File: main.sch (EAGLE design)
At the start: 28 parts, among them U1 MCP2551P-SOCKET, U2 STN1110SOCKET-28, Y1 16Mhz

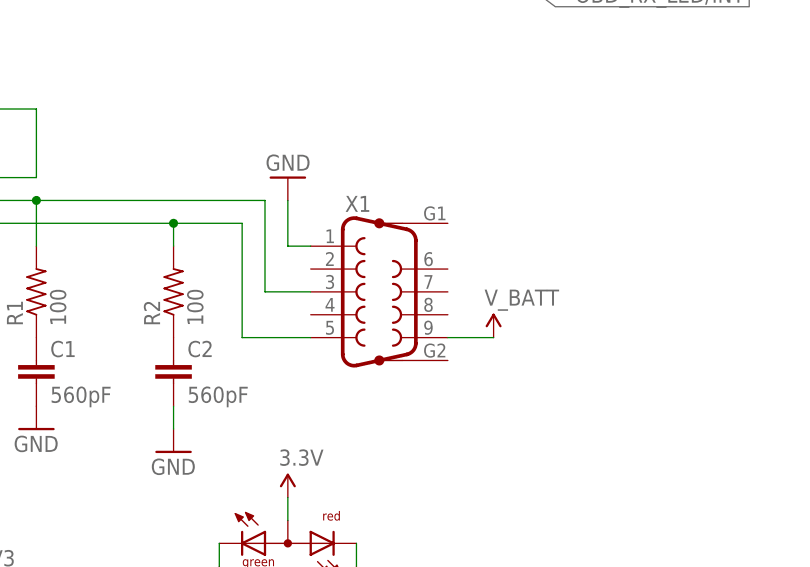
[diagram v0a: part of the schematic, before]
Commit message: Added some space and better routing
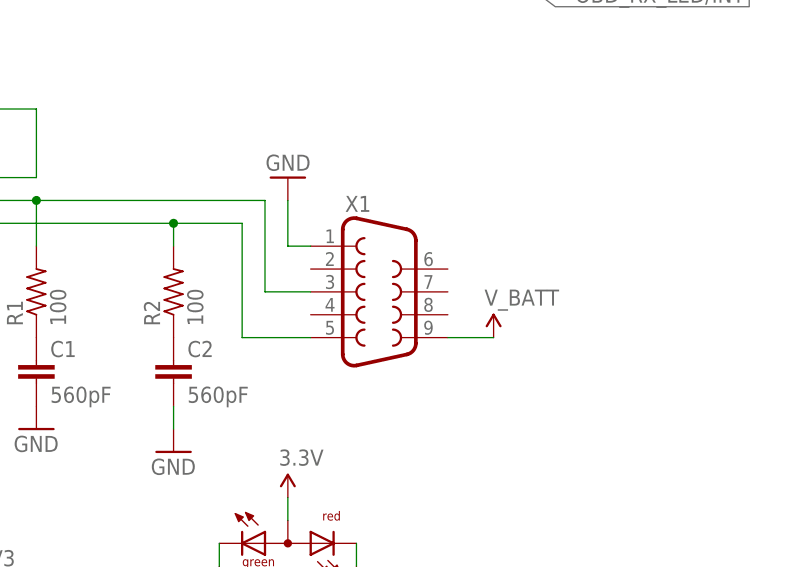
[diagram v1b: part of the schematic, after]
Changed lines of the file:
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@@
 <parts>
 <part name="ARDUINO1" library="post7_arduino" deviceset="ARDUINO" device=""/>
-<part name="X1" library="con-subd" deviceset="F09HP" device=""/>
+<part name="X1" library="con-subd" deviceset="F09" device="HP"/>
 <part name="GND28" library="SparkFun" deviceset="GND" device=""/>
 <part name="GND15" library="SparkFun" deviceset="GND" device=""/>

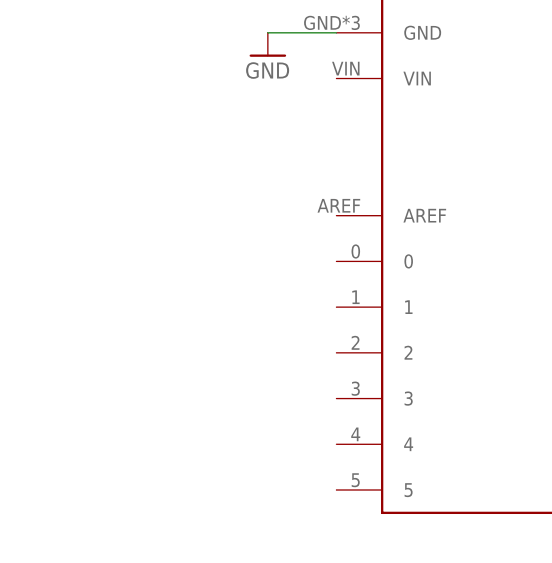
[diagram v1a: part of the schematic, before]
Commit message: Improved routing, added micro-sd slot
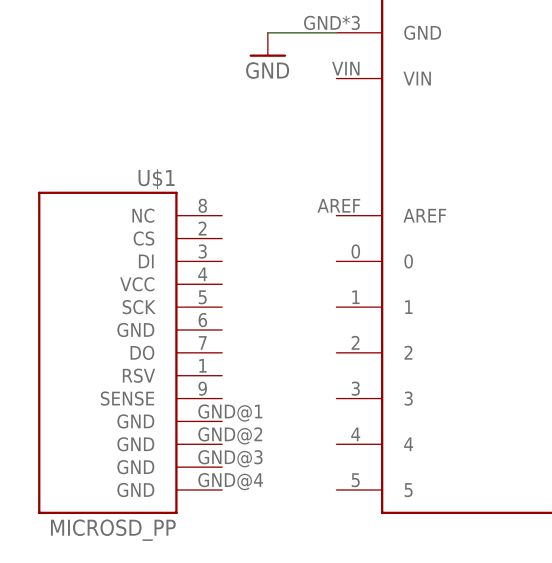
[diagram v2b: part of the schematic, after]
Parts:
- added U$1: MICROSD_PP, DE1594-v2:MICROSD_PP
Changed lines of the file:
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@@
 <part name="SUPPLY14" library="SparkFun-Aesthetics" deviceset="3.3V" device=""/>
 <part name="GND11" library="SparkFun-Aesthetics" deviceset="GND" device=""/>
+<part name="U$1" library="DE1594-v2" deviceset="MICROSD_PP" device=""/>
 </parts>
 <sheets>
@@
 <instance part="SUPPLY14" gate="G$1" x="-12.7" y="78.74"/>
 <instance part="GND11" gate="1" x="-12.7" y="68.58"/>
+<instance part="U$1" gate="G$1" x="-20.32" y="17.78"/>
 </instances>
 <busses>

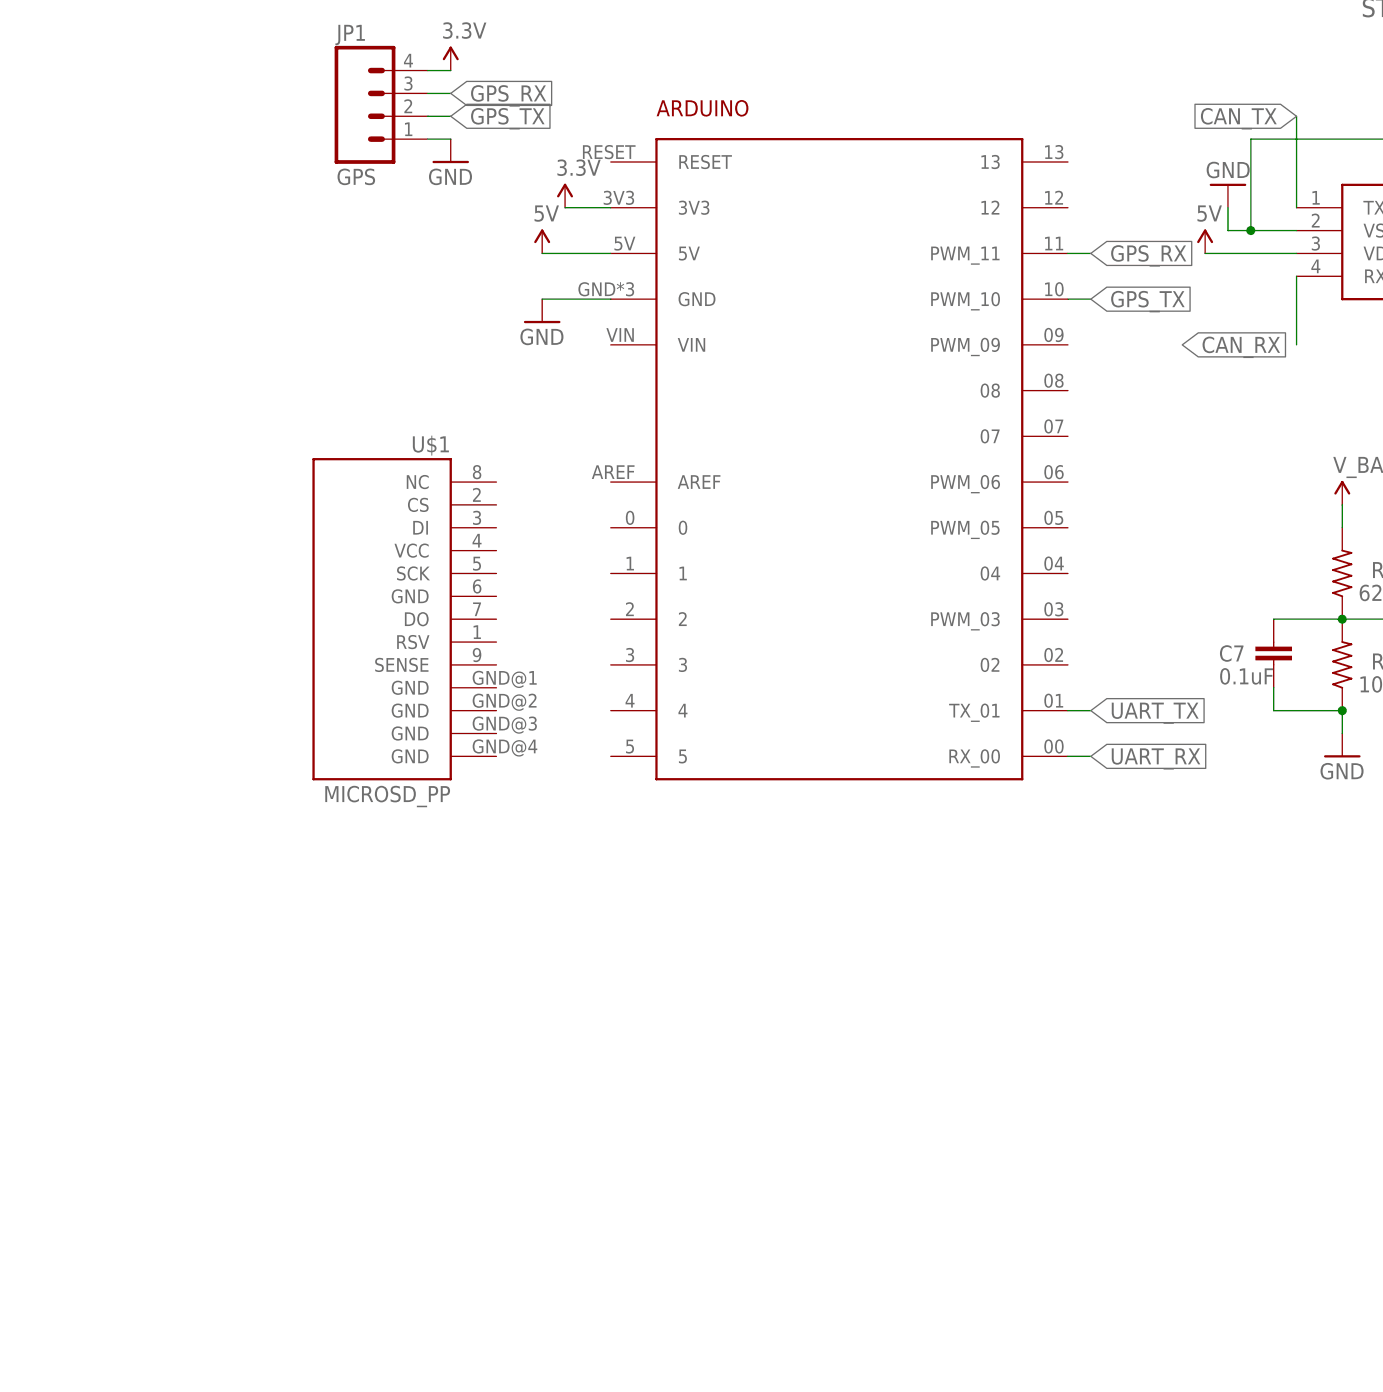
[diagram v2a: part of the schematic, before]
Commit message: Wired the SD card and level shifter
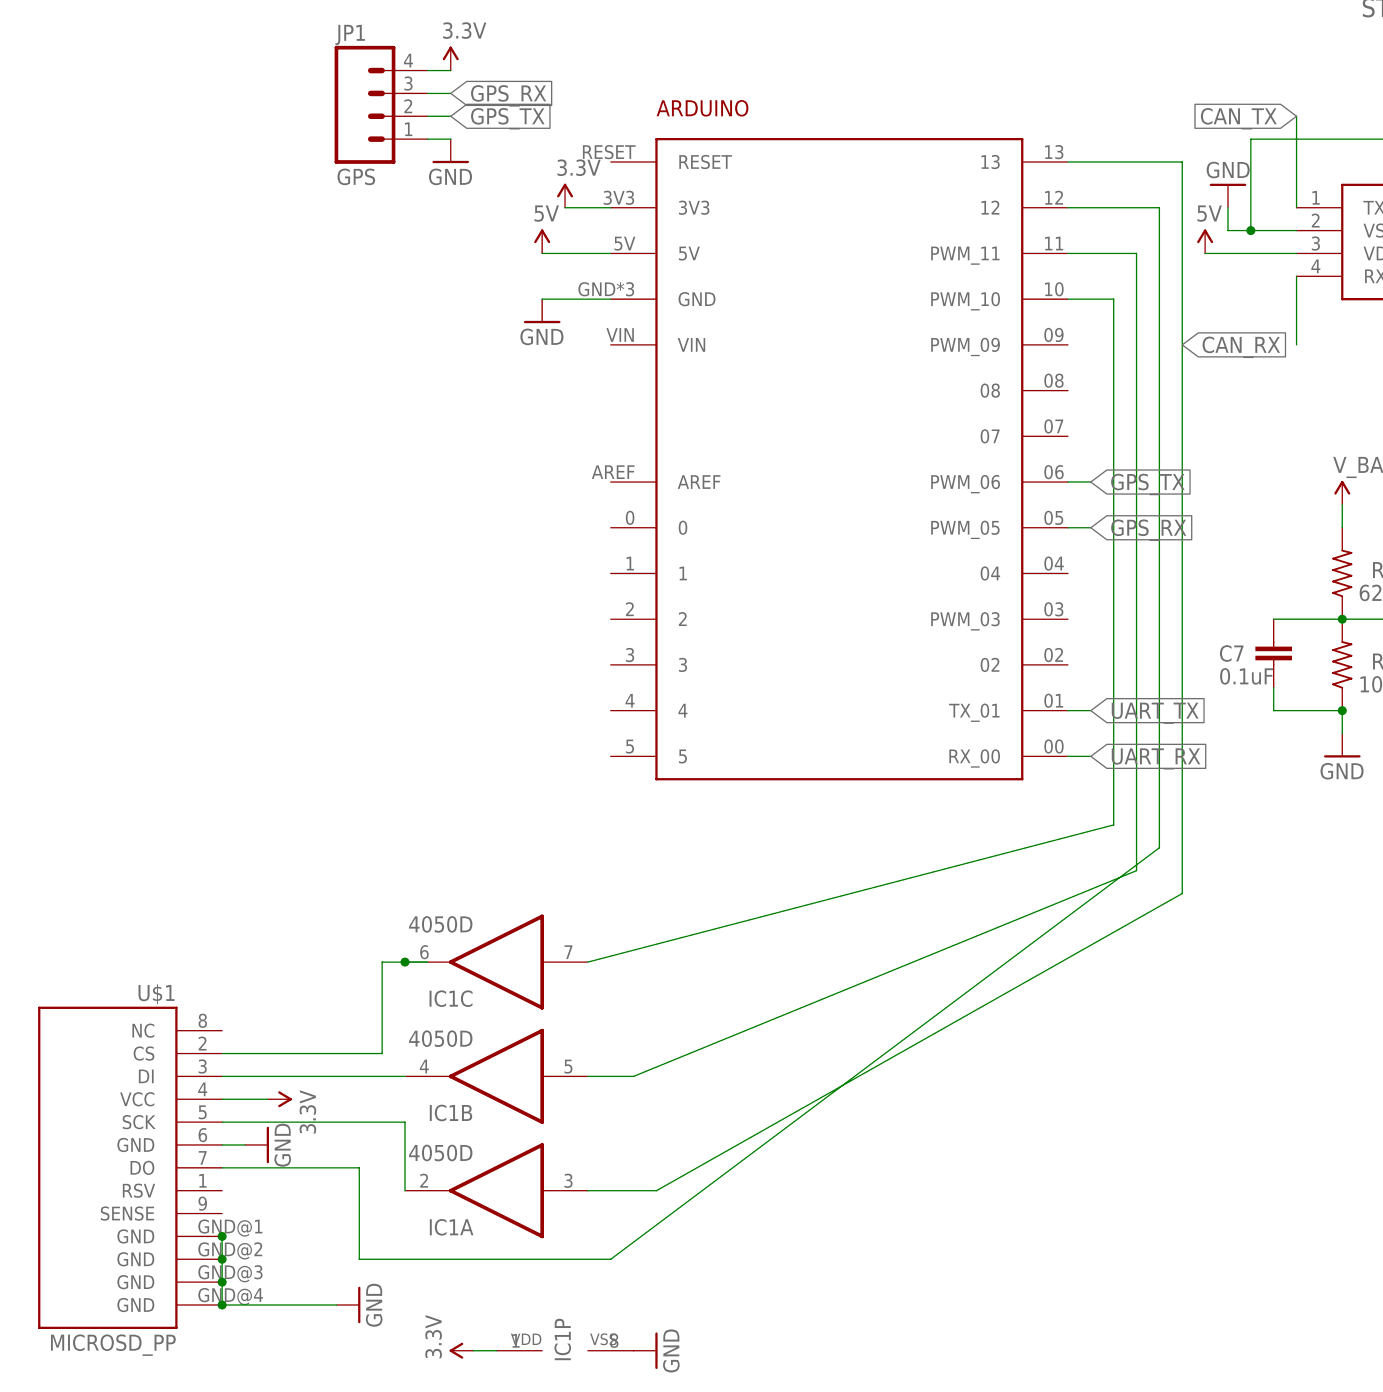
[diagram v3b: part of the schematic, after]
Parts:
- added IC1: 4050D, 40xx:4050D
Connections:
- new net N$13: IC1B.O, U$1.DI
- new net N$15: IC1C.O, U$1.CS
- new net N$16: ARDUINO1.13, IC1A.I
- new net N$17: IC1A.O, U$1.SCK
- new net N$18: ARDUINO1.PWM_10, IC1C.I
- new net N$19: ARDUINO1.12, U$1.DO
- new net N$20: ARDUINO1.PWM_11, IC1B.I
- net 3.3V: now also IC1P.VDD, U$1.VCC
- net GND: now also IC1P.VSS, U$1.GND, U$1.GND@1, U$1.GND@2, U$1.GND@3, U$1.GND@4
- net GPS_RX: now also ARDUINO1.PWM_05; no longer ARDUINO1.PWM_11
- net GPS_TX: now also ARDUINO1.PWM_06; no longer ARDUINO1.PWM_10
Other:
- moved on the sheet: U$1
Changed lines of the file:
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@@
 <part name="GND11" library="SparkFun-Aesthetics" deviceset="GND" device=""/>
 <part name="U$1" library="DE1594-v2" deviceset="MICROSD_PP" device=""/>
+<part name="IC1" library="40xx" deviceset="4050" device="D" value="4050D"/>
+<part name="SUPPLY15" library="SparkFun-Aesthetics" deviceset="3.3V" device=""/>
+<part name="GND12" library="SparkFun-Aesthetics" deviceset="GND" device=""/>
+<part name="GND13" library="SparkFun-Aesthetics" deviceset="GND" device=""/>
+<part name="SUPPLY16" library="SparkFun-Aesthetics" deviceset="3.3V" device=""/>
+<part name="GND14" library="SparkFun-Aesthetics" deviceset="GND" device=""/>
 </parts>
 <sheets>
@@
 <instance part="SUPPLY14" gate="G$1" x="-12.7" y="78.74"/>
 <instance part="GND11" gate="1" x="-12.7" y="68.58"/>
-<instance part="U$1" gate="G$1" x="-20.32" y="17.78"/>
+<instance part="U$1" gate="G$1" x="-50.8" y="-43.18"/>
+<instance part="IC1" gate="A" x="-7.62" y="-45.72" rot="R180"/>
+<instance part="IC1" gate="B" x="-7.62" y="-33.02" rot="R180"/>
+<instance part="IC1" gate="C" x="-7.62" y="-20.32" rot="R180"/>
+<instance part="IC1" gate="P" x="0" y="-63.5" rot="R90"/>
+<instance part="SUPPLY15" gate="G$1" x="-10.16" y="-63.5" rot="R90"/>
+<instance part="GND12" gate="1" x="10.16" y="-63.5" rot="R90"/>
+<instance part="GND13" gate="1" x="-22.86" y="-58.42" rot="R90"/>
+<instance part="SUPPLY16" gate="G$1" x="-33.02" y="-35.56" rot="R270"/>
+<instance part="GND14" gate="1" x="-33.02" y="-40.64" rot="R90"/>
 </instances>
 <busses>
@@
 <pinref part="GND11" gate="1" pin="GND"/>
 </segment>
+<segment>
+<pinref part="IC1" gate="P" pin="VSS"/>
+<pinref part="GND12" gate="1" pin="GND"/>
+</segment>
+<segment>
+<pinref part="U$1" gate="G$1" pin="GND@1"/>
+<wire x1="-38.1" y1="-50.8" x2="-38.1" y2="-53.34" width="0.1524" layer="91"/>
+<pinref part="GND13" gate="1" pin="GND"/>
+<pinref part="U$1" gate="G$1" pin="GND@2"/>
+<junction x="-38.1" y="-53.34"/>
+<wire x1="-38.1" y1="-53.34" x2="-38.1" y2="-55.88" width="0.1524" layer="91"/>
+<pinref part="U$1" gate="G$1" pin="GND@3"/>
+<junction x="-38.1" y="-55.88"/>
+<wire x1="-38.1" y1="-55.88" x2="-38.1" y2="-58.42" width="0.1524" layer="91"/>
+<pinref part="U$1" gate="G$1" pin="GND@4"/>
+<junction x="-38.1" y="-58.42"/>
+<wire x1="-38.1" y1="-58.42" x2="-25.4" y2="-58.42" width="0.1524" layer="91"/>
+<junction x="-38.1" y="-50.8"/>
+</segment>
+<segment>
+<pinref part="U$1" gate="G$1" pin="GND"/>
+<pinref part="GND14" gate="1" pin="GND"/>
+<wire x1="-38.1" y1="-40.64" x2="-35.56" y2="-40.64" width="0.1524" layer="91"/>
+</segment>
 </net>
 <net name="N$1" class="0">
@@
 <wire x1="-15.24" y1="78.74" x2="-12.7" y2="78.74" width="0.1524" layer="91"/>
 <pinref part="SUPPLY14" gate="G$1" pin="3.3V"/>
+</segment>
+<segment>
+<pinref part="IC1" gate="P" pin="VDD"/>
+<pinref part="SUPPLY15" gate="G$1" pin="3.3V"/>
+<wire x1="-10.16" y1="-63.5" x2="-7.62" y2="-63.5" width="0.1524" layer="91"/>
+</segment>
+<segment>
+<pinref part="U$1" gate="G$1" pin="VCC"/>
+<pinref part="SUPPLY16" gate="G$1" pin="3.3V"/>
+<wire x1="-38.1" y1="-35.56" x2="-33.02" y2="-35.56" width="0.1524" layer="91"/>
 </segment>
 </net>
@@
 </segment>
 <segment>
-<pinref part="ARDUINO1" gate="G$1" pin="PWM_10"/>
-<wire x1="55.88" y1="53.34" x2="58.42" y2="53.34" width="0.1524" layer="91"/>
-<label x="58.42" y="53.34" size="1.778" layer="95" xref="yes"/>
+<pinref part="ARDUINO1" gate="G$1" pin="PWM_06"/>
+<wire x1="55.88" y1="33.02" x2="58.42" y2="33.02" width="0.1524" layer="91"/>
+<label x="58.42" y="33.02" size="1.778" layer="95" rot="MR180" xref="yes"/>
 </segment>
 </net>
@@
 </segment>
 <segment>
+<pinref part="ARDUINO1" gate="G$1" pin="PWM_05"/>
+<wire x1="55.88" y1="27.94" x2="58.42" y2="27.94" width="0.1524" layer="91"/>
+<label x="58.42" y="27.94" size="1.778" layer="95" xref="yes"/>
+</segment>
+</net>
+<net name="N$15" class="0">
+<segment>
+<wire x1="-20.32" y1="-20.32" x2="-17.78" y2="-20.32" width="0.1524" layer="91"/>
+<pinref part="U$1" gate="G$1" pin="CS"/>
+<wire x1="-17.78" y1="-20.32" x2="-15.24" y2="-20.32" width="0.1524" layer="91"/>
+<wire x1="-20.32" y1="-20.32" x2="-20.32" y2="-30.48" width="0.1524" layer="91"/>
+<wire x1="-20.32" y1="-30.48" x2="-38.1" y2="-30.48" width="0.1524" layer="91"/>
+<pinref part="IC1" gate="C" pin="O"/>
+<junction x="-17.78" y="-20.32"/>
+</segment>
+</net>
+<net name="N$16" class="0">
+<segment>
+<wire x1="68.58" y1="-12.7" x2="68.58" y2="68.58" width="0.1524" layer="91"/>
+<pinref part="ARDUINO1" gate="G$1" pin="13"/>
+<wire x1="68.58" y1="68.58" x2="55.88" y2="68.58" width="0.1524" layer="91"/>
+<pinref part="IC1" gate="A" pin="I"/>
+<wire x1="68.58" y1="-12.7" x2="10.16" y2="-45.72" width="0.1524" layer="91"/>
+<wire x1="10.16" y1="-45.72" x2="2.54" y2="-45.72" width="0.1524" layer="91"/>
+</segment>
+</net>
+<net name="N$13" class="0">
+<segment>
+<pinref part="U$1" gate="G$1" pin="DI"/>
+<pinref part="IC1" gate="B" pin="O"/>
+<wire x1="-38.1" y1="-33.02" x2="-17.78" y2="-33.02" width="0.1524" layer="91"/>
+</segment>
+</net>
+<net name="N$17" class="0">
+<segment>
+<pinref part="U$1" gate="G$1" pin="SCK"/>
+<wire x1="-38.1" y1="-38.1" x2="-17.78" y2="-38.1" width="0.1524" layer="91"/>
+<pinref part="IC1" gate="A" pin="O"/>
+<wire x1="-17.78" y1="-38.1" x2="-17.78" y2="-45.72" width="0.1524" layer="91"/>
+</segment>
+</net>
+<net name="N$18" class="0">
+<segment>
+<pinref part="ARDUINO1" gate="G$1" pin="PWM_10"/>
+<wire x1="55.88" y1="53.34" x2="60.96" y2="53.34" width="0.1524" layer="91"/>
+<wire x1="60.96" y1="53.34" x2="60.96" y2="-5.08" width="0.1524" layer="91"/>
+<pinref part="IC1" gate="C" pin="I"/>
+<wire x1="60.96" y1="-5.08" x2="2.54" y2="-20.32" width="0.1524" layer="91"/>
+</segment>
+</net>
+<net name="N$19" class="0">
+<segment>
+<pinref part="ARDUINO1" gate="G$1" pin="12"/>
+<wire x1="55.88" y1="63.5" x2="66.04" y2="63.5" width="0.1524" layer="91"/>
+<wire x1="66.04" y1="63.5" x2="66.04" y2="-7.62" width="0.1524" layer="91"/>
+<wire x1="66.04" y1="-7.62" x2="5.08" y2="-53.34" width="0.1524" layer="91"/>
+<wire x1="5.08" y1="-53.34" x2="-22.86" y2="-53.34" width="0.1524" layer="91"/>
+<pinref part="U$1" gate="G$1" pin="DO"/>
+<wire x1="-22.86" y1="-53.34" x2="-22.86" y2="-43.18" width="0.1524" layer="91"/>
+<wire x1="-22.86" y1="-43.18" x2="-38.1" y2="-43.18" width="0.1524" layer="91"/>
+</segment>
+</net>
+<net name="N$20" class="0">
+<segment>
 <pinref part="ARDUINO1" gate="G$1" pin="PWM_11"/>
-<wire x1="55.88" y1="58.42" x2="58.42" y2="58.42" width="0.1524" layer="91"/>
-<label x="58.42" y="58.42" size="1.778" layer="95" xref="yes"/>
-</segment>
-</net>
+<wire x1="55.88" y1="58.42" x2="63.5" y2="58.42" width="0.1524" layer="91"/>
+<wire x1="63.5" y1="58.42" x2="63.5" y2="-10.16" width="0.1524" layer="91"/>
+<pinref part="IC1" gate="B" pin="I"/>
+<wire x1="63.5" y1="-10.16" x2="7.62" y2="-33.02" width="0.1524" layer="91"/>
+<wire x1="7.62" y1="-33.02" x2="2.54" y2="-33.02" width="0.1524" layer="91"/>
+</segment>
+</net>

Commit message: Better layout...
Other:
- note added: "OBD Tx/Rx"
- note added: "Voltage-sense"
- moved on the sheet: C1, C2, C3, C4, C5, C6, C7, D1, D2, IC1A, IC1B, IC1C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

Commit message: Finished wiring, added external v-supply
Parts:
- removed LD1: (no value), led:DUOLED-RG-A
- added JP2: 5V Transformer, SparkFun-Connectors:M04LOCK
- added LED1: L-115WEGW-CA, led:L-115WEGW-CA
- U$1: value MICROSD_PP -> MICROSD
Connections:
- net 3.3V: now also LED1.A; no longer LD1.A
- net 5V: now also JP2.1
- net GND: now also JP2.2, JP2.3
- net N$10: now also LED1.CG; no longer LD1.CG
- net N$11: now also LED1.CR; no longer LD1.CR
- net V_BATT: now also JP2.4
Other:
- moved on the sheet: C1, C2, R1, R12, R2, X1
